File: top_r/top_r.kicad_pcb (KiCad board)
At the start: 2 copper layers, 127 x 102.6 mm, 21 parts, among them SW23 SW_Push, SW24 SW_Push, SW25 SW_Push, SW26 SW_Push, SW27 SW_Push, SW28 SW_Push, SW29 SW_Push, SW30 SW_Push, SW31 SW_Push, SW32 SW_Push, SW33 SW_Push, SW34 SW_Push, SW35 SW_Push, SW36 SW_Push, SW37 SW_Push, SW38 SW_Push, SW39 SW_Push, SW40 SW_Push, SW41 SW_Push, SW42 SW_Push, SW43 SW_Push

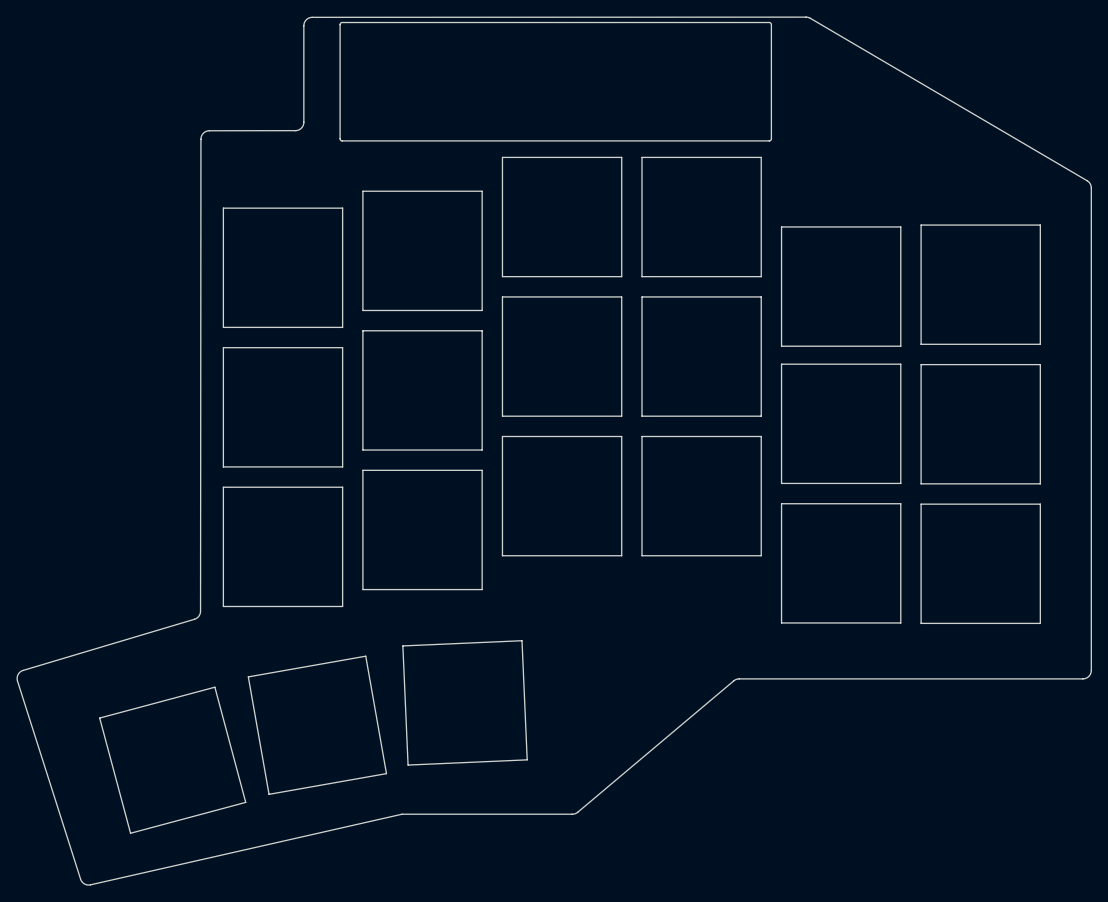
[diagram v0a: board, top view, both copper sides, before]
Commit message: feat: add screw
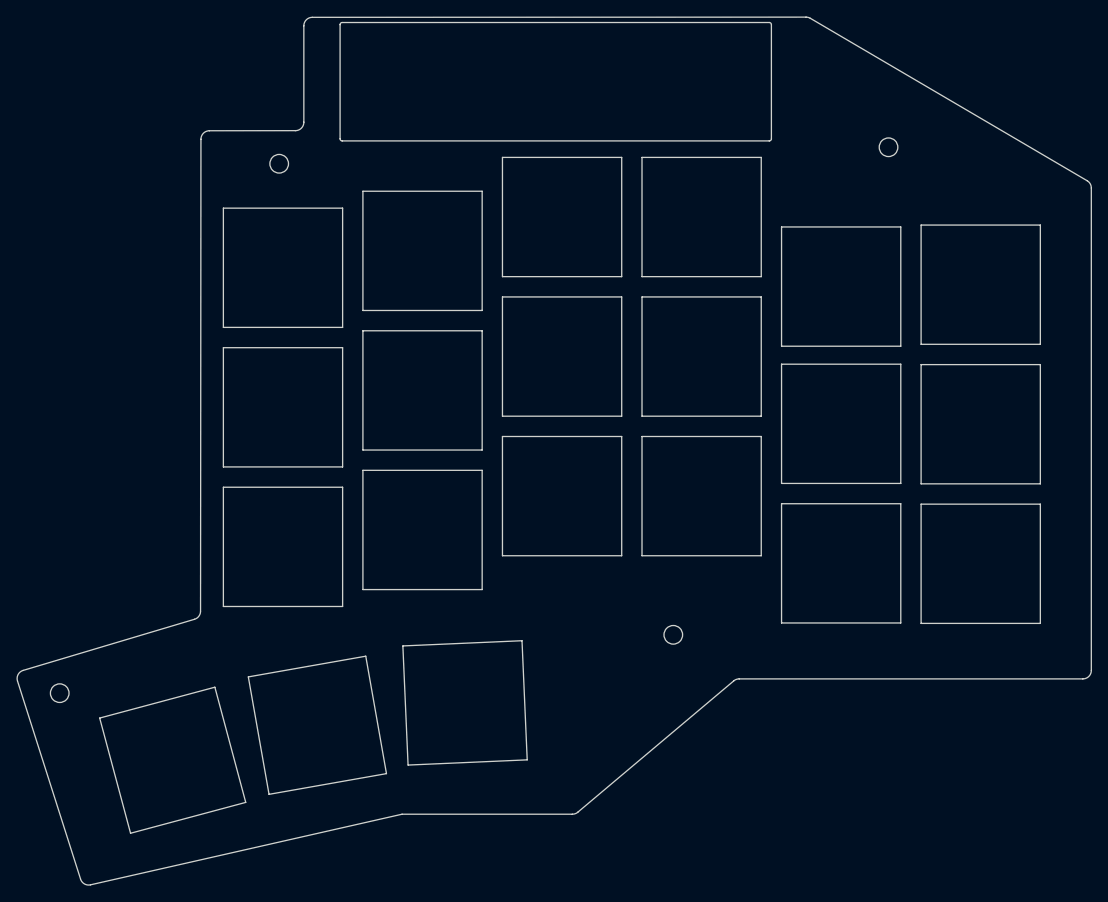
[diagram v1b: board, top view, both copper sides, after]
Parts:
- added Ref**: Val**, kbd_Hole:m2_Screw_Hole, F.Cu at (76.5, 65.0)
- added Ref**: Val**, kbd_Hole:m2_Screw_Hole, F.Cu at (50.5, 127.7)
- added Ref**: Val**, kbd_Hole:m2_Screw_Hole, F.Cu at (123.0, 120.8)
- added Ref**: Val**, kbd_Hole:m2_Screw_Hole, F.Cu at (148.5, 63.1)
